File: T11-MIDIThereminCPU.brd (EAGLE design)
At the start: 103.8 x 81.3 mm, 62 parts, among them IC1 UA78M05DCY, IC4 QUAD_OPAMPD, IC5 4069D, J1 DCJ0202, Q1 16MHz, U1 ATMEGA328P-AU

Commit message: Board creation
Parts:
- moved C10 97.1 mm to (3.81, 22.9), turned to 90 degrees
- moved C9 88.7 mm to (91.4, 20.3), turned to 270 degrees
- moved C7 87.8 mm to (22.9, 21.6), turned to 270 degrees
- moved R21 85.9 mm to (97.8, 38.1), turned to 270 degrees
- moved R10 83.2 mm to (86.4, 24.1), turned to 270 degrees
- moved LED1 81.3 mm to (95.2, 76.2)
- moved R3 71.5 mm to (17.8, 24.1), turned to 90 degrees
- moved LED2 70.3 mm to (95.2, 68.6)
- moved R8 70.0 mm to (27.9, 24.1), turned to 270 degrees
- moved JP3 70.0 mm to (27.9, 48.3), turned to 0 degrees
- moved U$4 67.6 mm to (52.1, 24.1), turned to 90 degrees
- moved JP2 64.4 mm to (29.2, 39.4), turned to 0 degrees
- moved C5 64.1 mm to (17.8, 34.3)
- moved LED3 60.1 mm to (95.2, 62.2)
- moved R13 55.3 mm to (85.1, 76.2), turned to 0 degrees
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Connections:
- net GND: now also IC4.12, IC4.13, IC5.11, IC5.13, IC5.5, IC5.9
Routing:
- net GND: track 0.00 -> 535.0 mm
- net +5V: track 0.00 -> 202.9 mm, vias 0 -> 2
- net +12V: track 0.00 -> 154.0 mm
- net ANALOG_IN_1: track 0.00 -> 130.9 mm, vias 0 -> 2
- net MOSI: track 0.00 -> 117.6 mm
- net ANALOG_IN_2: track 0.00 -> 116.7 mm, vias 0 -> 1
- net ANALOG_IN_3: track 0.00 -> 114.7 mm, vias 0 -> 1
- net SIGNAL_OUT_2: track 0.00 -> 70.4 mm, vias 0 -> 1
- net LED_1: track 0.00 -> 66.4 mm
- net PC3: track 0.00 -> 63.6 mm, vias 0 -> 2
- net TX: track 0.00 -> 62.8 mm, vias 0 -> 1
- net ADC6: track 0.00 -> 60.7 mm, vias 0 -> 4
- net SIGNAL_OUT_1: track 0.00 -> 60.4 mm, vias 0 -> 2
- net PC5: track 0.00 -> 57.0 mm, vias 0 -> 1
- net LED_5: track 0.00 -> 56.4 mm
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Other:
- board size 103.8 x 81.3 mm -> 100 x 80 mm

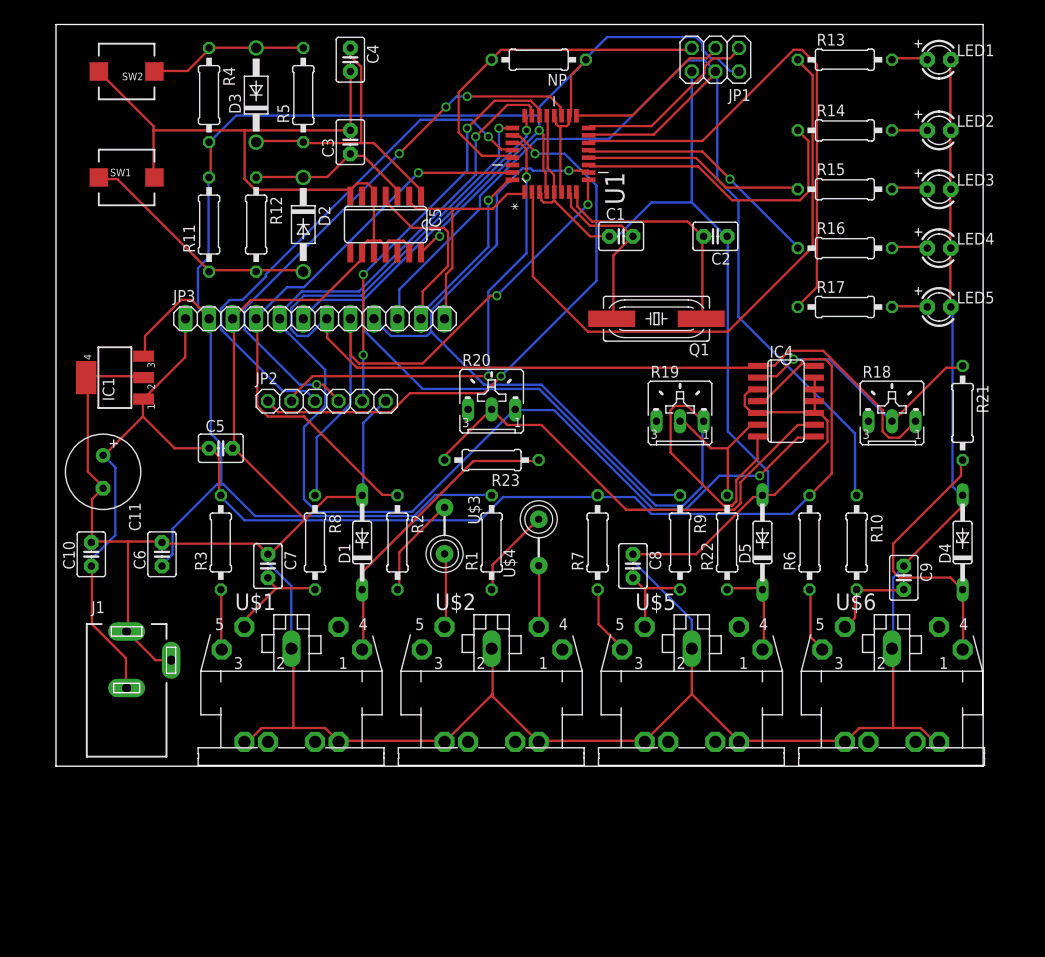
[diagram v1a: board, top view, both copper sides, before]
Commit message: Changed resistors and caps to smd
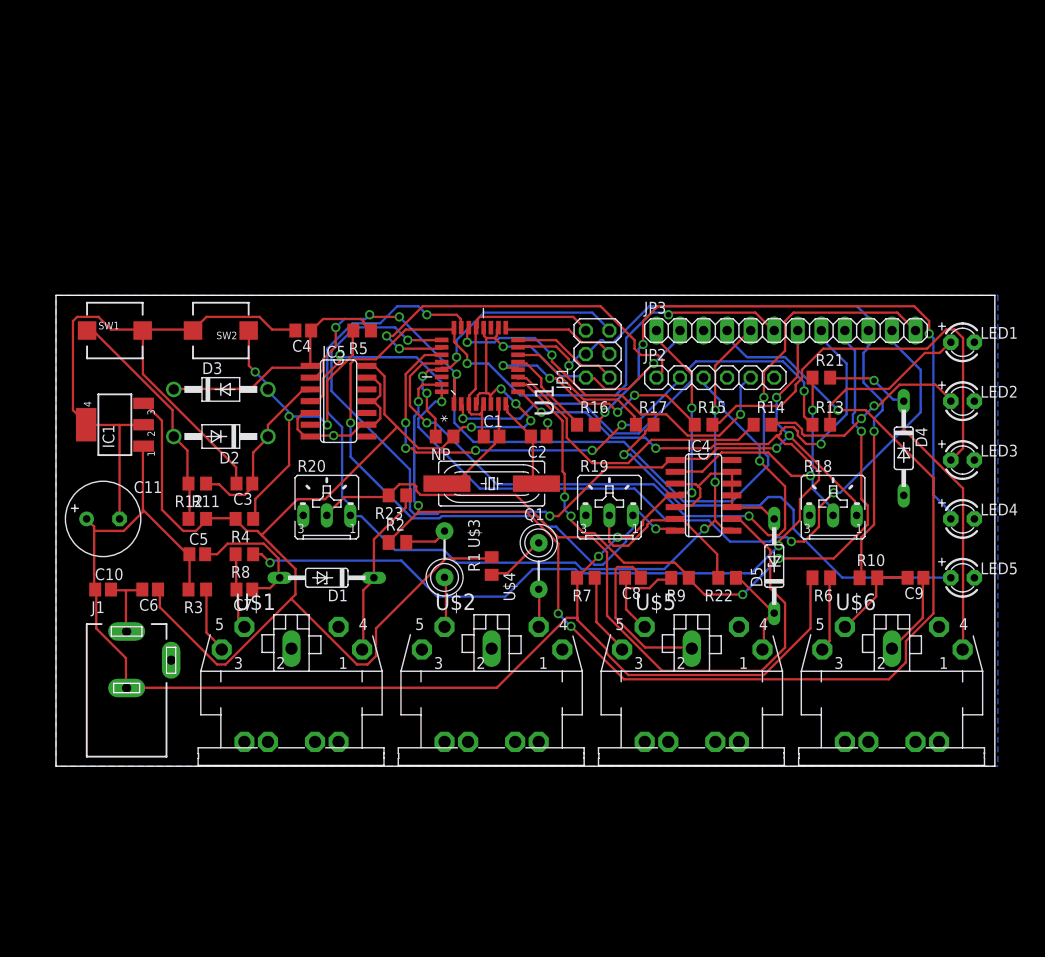
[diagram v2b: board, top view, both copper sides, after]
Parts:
- C1, C10, C2, C3, C4, C5, C6, C7, C8, C9: device capacitor-wima:C2.5-3 -> adafruit:C0805
- NP, R1, R11, R12, R13, R14, R15, R16, R17, R21, R22, R23, R3, R4, R5, R7, R8, R9: device resistor:0207/10 -> resistor:R0805
- R10, R2, R6: device resistor:0207/10 -> resistor:M0805
- moved JP3 50.8 mm to (78.7, 47.0)
- moved R4 45.9 mm to (20.3, 26.7), turned to 180 degrees
- moved JP2 42.0 mm to (71.1, 41.9)
- moved NP 41.9 mm to (41.9, 35.6)
- moved R13 39.5 mm to (82.5, 36.8)
- moved C3 38.6 mm to (20.3, 30.5), turned to 180 degrees
- moved JP1 34.2 mm to (58.4, 44.5), turned to 90 degrees
- moved R16 33.8 mm to (57.1, 36.8)
- moved R14 33.0 mm to (76.2, 36.8)
- moved D3 32.0 mm to (17.8, 40.6), turned to 0 degrees
- moved R11 31.8 mm to (15.2, 26.7), turned to 0 degrees
- moved LED1 30.6 mm to (97.8, 45.7)
- moved SW2 29.7 mm to (17.8, 47.0)
- moved C4 29.6 mm to (26.7, 47.0), turned to 180 degrees
- moved R15 29.6 mm to (69.8, 36.8)
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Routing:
- net GND: track 535.0 -> 195.3 mm, vias 0 -> 2
- net INT1: track 26.5 -> 102.8 mm, vias 0 -> 5
- net TX: track 62.8 -> 136.6 mm, vias 1 -> 5
- net SIGNAL_OUT_1: track 60.4 -> 129.3 mm, vias 2 -> 5
- net INT0: track 38.6 -> 103.1 mm, vias 1 -> 4
- net N$16: track 3.97 -> 67.8 mm, vias 0 -> 3
- net ADC6: track 60.7 -> 0.00 mm, vias 4 -> 0
- net MOSI: track 117.6 -> 73.0 mm, vias 0 -> 2
- net N$17: track 3.89 -> 47.4 mm, vias 0 -> 1
- net N$15: track 4.06 -> 46.4 mm
- net LED_5: track 56.4 -> 16.3 mm
- net N$18: track 52.0 -> 81.3 mm
- net +5V: track 202.9 -> 176.0 mm, vias 2 -> 6
- net ANALOG_IN_1: track 130.9 -> 105.3 mm, vias 2 -> 4
- net N$4: track 17.2 -> 39.6 mm, vias 0 -> 3
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- added copper zone on layer 16, net GND
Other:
- board size 100 x 80 mm -> 101.3 x 50.8 mm

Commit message: Add files via upload
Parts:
- added C12, C13: 0.1u, adafruit:C0805
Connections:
- net +5V: now also C12.1, C13.1
- net GND: now also C12.2, C13.2
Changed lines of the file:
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@@
 <?xml version="1.0" encoding="utf-8"?>
 <!DOCTYPE eagle SYSTEM "eagle.dtd">
-<eagle version="7.6.0">
+<eagle version="7.7.0">
 <drawing>
 <settings>
@@
 <attribute name="OC_NEWARK" value="14R4631" x="45.72" y="43.18" size="1.778" layer="27" rot="R90" display="off"/>
 </element>
+<element name="C12" library="adafruit" package="C0805" value="0.1u" x="-2.54" y="-11.43"/>
+<element name="C13" library="adafruit" package="C0805" value="0.1u" x="-2.54" y="-17.78"/>
 </elements>
 <signals>
@@
 <via x="53.0352" y="37.0332" extent="1-16" drill="0.6096"/>
 <via x="29.9466" y="35.6616" extent="1-16" drill="0.6096"/>
-<wire x1="62.1792" y1="21.4884" x2="66.7766" y2="27.94" width="0" layer="19" extent="1-1"/>
+<contactref element="C12" pad="2"/>
+<contactref element="C13" pad="2"/>
+<wire x1="-1.69" y1="-11.43" x2="-1.69" y2="-17.78" width="0" layer="19" extent="1-1"/>
+<wire x1="20.32" y1="2.62" x2="-1.69" y2="-11.43" width="0" layer="19" extent="1-1"/>
+<wire x1="66.7766" y1="27.94" x2="62.1792" y2="21.4884" width="0" layer="19" extent="1-1"/>
 <wire x1="69.85" y1="46.99" x2="77.47" y2="41.91" width="0" layer="19" extent="1-1"/>
 <wire x1="44.5262" y1="39.0652" x2="34.9758" y2="38.6334" width="0" layer="19" extent="1-1"/>
@@
 <via x="51.2064" y="37.2618" extent="1-16" drill="0.6096"/>
 <via x="44.8056" y="36.576" extent="1-16" drill="0.6096"/>
+<contactref element="C12" pad="1"/>
+<contactref element="C13" pad="1"/>
+<contactref element="C13" pad="1"/>
+<wire x1="-3.39" y1="-11.43" x2="17.3736" y2="10.9728" width="0" layer="19" extent="1-1"/>
+<wire x1="-3.39" y1="-17.78" x2="-3.39" y2="-11.43" width="0" layer="19" extent="1-1"/>
 </signal>
 <signal name="TX">

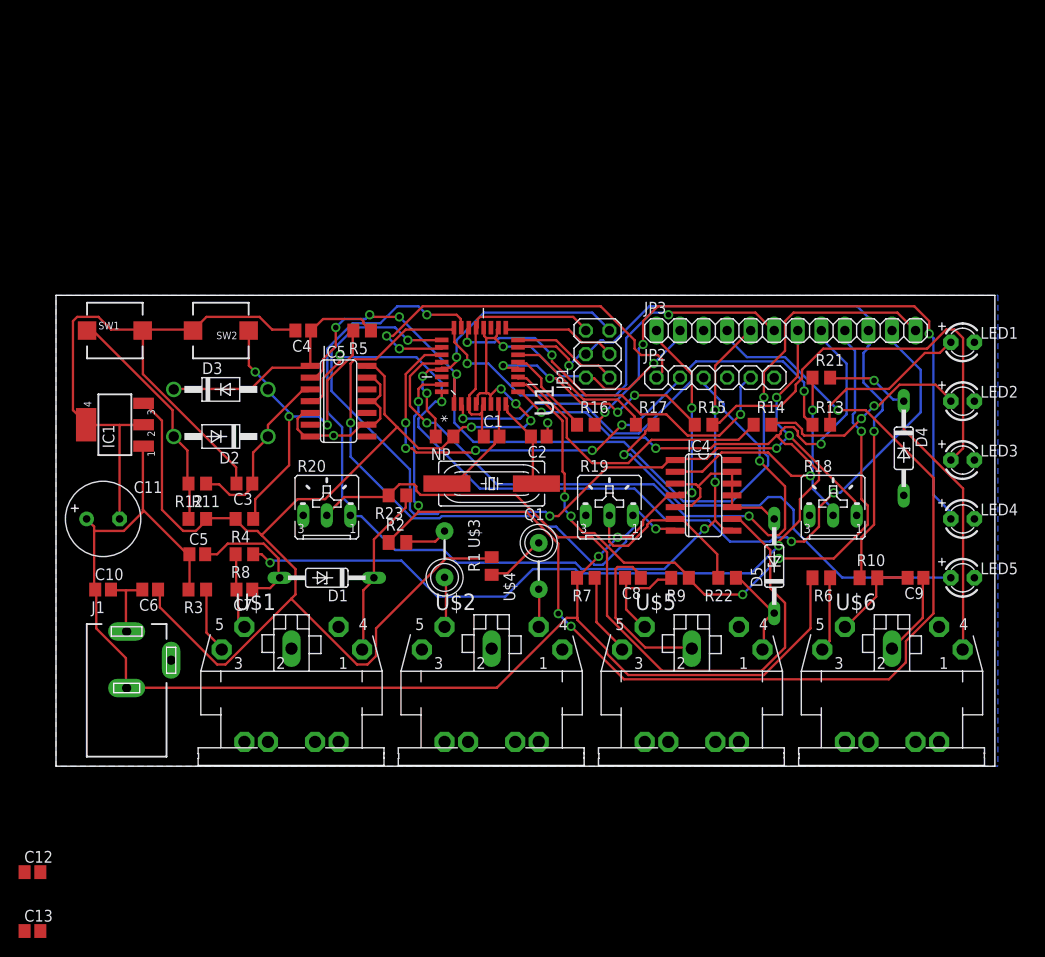
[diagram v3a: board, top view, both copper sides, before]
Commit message: Improved routing, coupling caps added
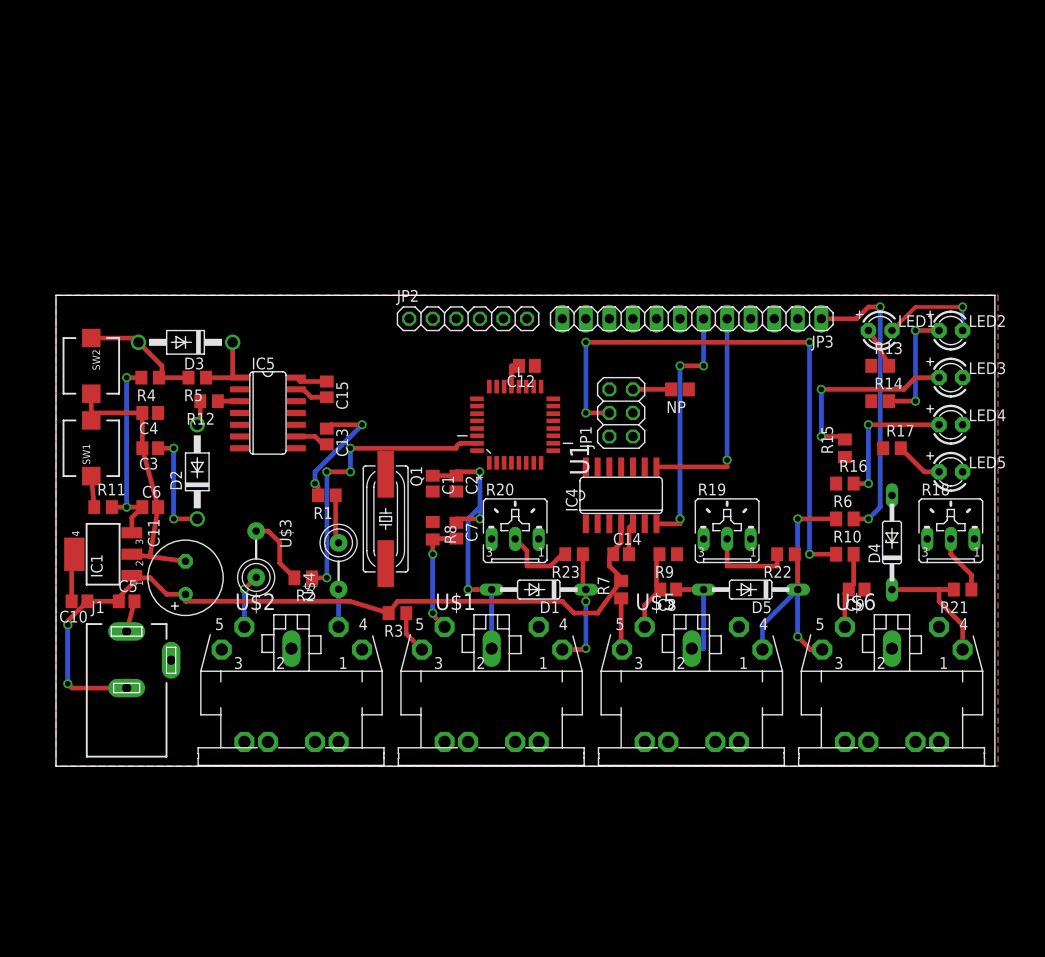
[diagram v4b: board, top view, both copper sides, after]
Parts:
- added C14, C15: 0.1u, adafruit:C0805
- moved C12 76.3 mm to (50.8, 43.2), turned to 180 degrees
- moved C13 62.1 mm to (29.2, 35.6), turned to 270 degrees
- moved R16 28.7 mm to (85.1, 30.5)
- moved R21 27.5 mm to (97.8, 19.1), turned to 180 degrees
- moved JP2 27.4 mm to (44.5, 48.3)
- moved R17 26.8 mm to (90.2, 34.3)
- moved NP 25.9 mm to (67.3, 40.6)
- moved C7 23.7 mm to (43.2, 25.4), turned to 270 degrees
- moved D1 22.9 mm to (52.1, 19.1)
- moved R3 21.7 mm to (36.8, 16.5)
- moved U$1 21.6 mm to (47.0, 0.00)
- moved U$2 21.6 mm to (25.4, 0.00)
- moved U$4 21.6 mm to (30.5, 21.6)
- moved R20 20.5 mm to (49.5, 25.4)
- moved R8 20.5 mm to (40.6, 25.4), turned to 270 degrees
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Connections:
- net +12V: now also C14.1
- net +5V: now also C15.1
- net GND: now also C14.2, C15.2
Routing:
- net +5V: track 176.0 -> 39.4 mm, vias 6 -> 4
- net SIGNAL_OUT_1: track 129.3 -> 0.00 mm, vias 5 -> 0
- net TX: track 136.6 -> 32.0 mm, vias 5 -> 4
- net ANALOG_IN_3: track 103.7 -> 0.00 mm, vias 5 -> 0
- net INT0: track 103.1 -> 0.00 mm, vias 4 -> 0
- net INT1: track 102.8 -> 0.00 mm, vias 5 -> 0
- net GND: track 195.3 -> 106.6 mm, vias 2 -> 4
- net ANALOG_IN_2: track 114.1 -> 27.2 mm, vias 4 -> 3
- net ANALOG_IN_1: track 105.3 -> 23.6 mm, vias 4 -> 1
- net SIGNAL_OUT_2: track 78.4 -> 0.00 mm, vias 5 -> 0
- net PC5: track 73.8 -> 0.00 mm, vias 3 -> 0
- net N$18: track 81.3 -> 8.10 mm
- net N$16: track 67.8 -> 15.6 mm, vias 3 -> 2
- net +12V: track 171.6 -> 119.7 mm
- net LED_1: track 50.8 -> 0.00 mm, vias 2 -> 0
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- added copper zone on layer 1, net GND

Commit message: Improved routing, added coupling caps
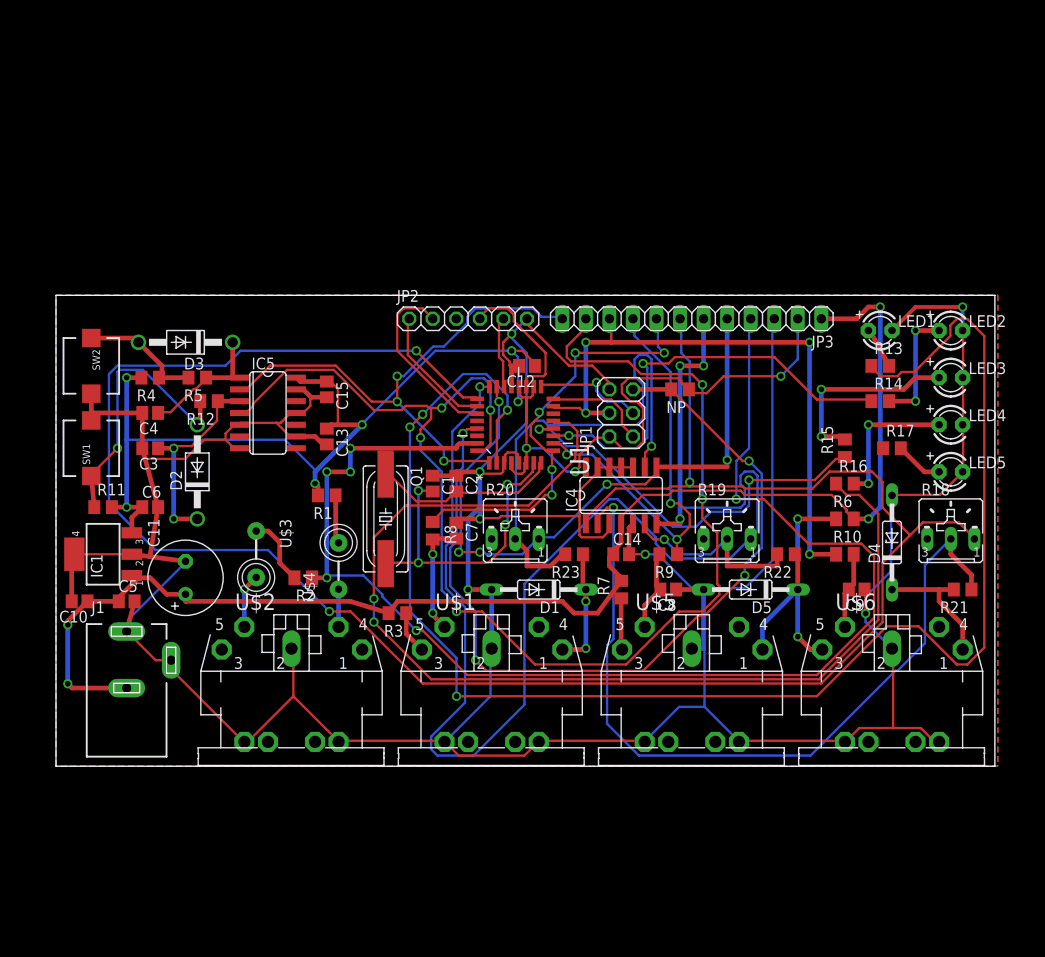
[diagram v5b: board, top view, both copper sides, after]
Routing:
- net GND: track 106.6 -> 447.7 mm, vias 4 -> 7
- net ANALOG_IN_3: track 0.00 -> 230.8 mm, vias 0 -> 3
- net LED_1: track 0.00 -> 165.5 mm, vias 0 -> 4
- net INT0: track 0.00 -> 143.1 mm, vias 0 -> 6
- net ANALOG_IN_2: track 27.2 -> 148.6 mm, vias 3 -> 4
- net +5V: track 39.4 -> 160.4 mm, vias 4 -> 9
- net LED_4: track 0.00 -> 117.6 mm, vias 0 -> 2
- net TX: track 32.0 -> 142.6 mm, vias 4 -> 6
- net RST: track 4.13 -> 91.1 mm, vias 0 -> 4
- net N$19: track 6.38 -> 86.0 mm, vias 0 -> 1
- net INT1: track 0.00 -> 57.6 mm, vias 0 -> 3
- net SIGNAL_OUT_2: track 0.00 -> 47.0 mm, vias 0 -> 3
- net SIGNAL_OUT_1: track 0.00 -> 46.6 mm, vias 0 -> 5
- net N$18: track 8.10 -> 54.7 mm, vias 0 -> 1
- net LED_2: track 0.00 -> 46.3 mm, vias 0 -> 2
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
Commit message: Fixed DRC errors
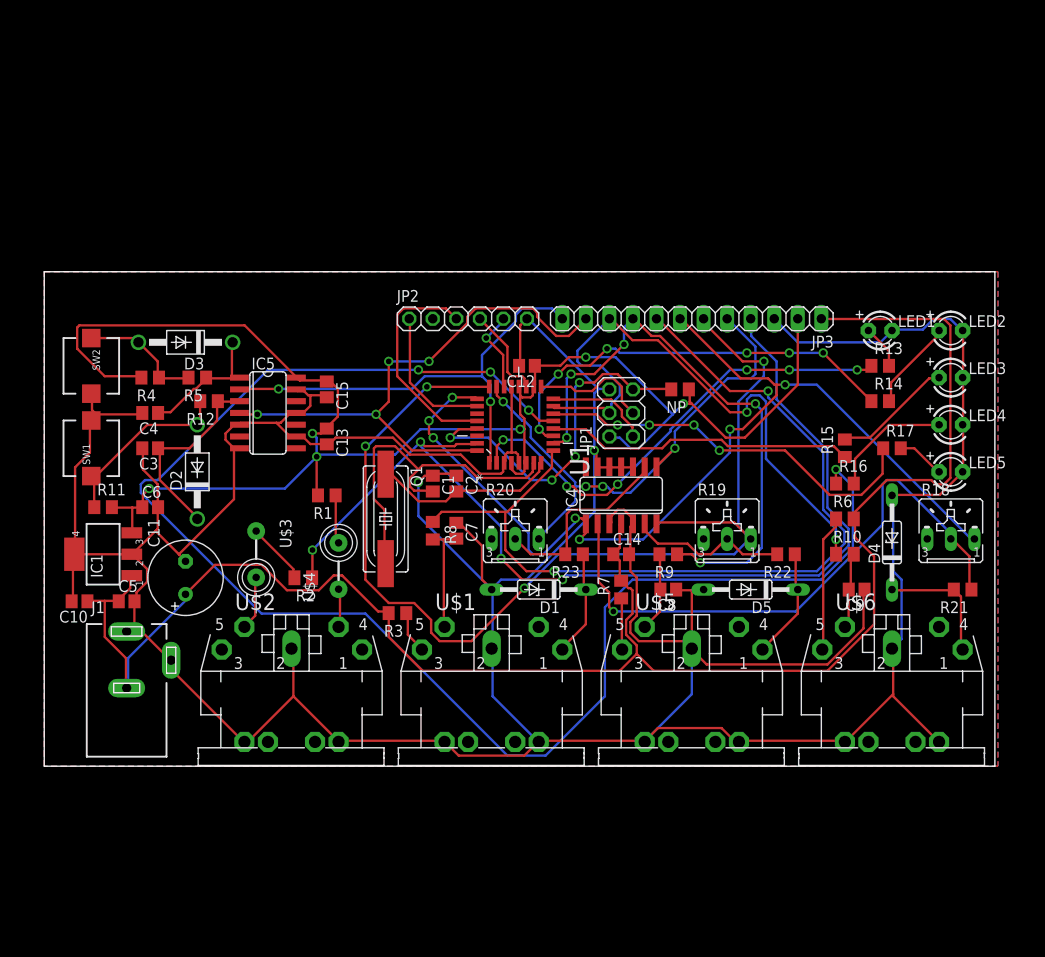
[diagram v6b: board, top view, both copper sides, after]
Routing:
- net ANALOG_IN_3: track 230.8 -> 107.2 mm, vias 3 -> 7
- net LED_1: track 165.5 -> 51.1 mm, vias 4 -> 6
- net INT0: track 143.1 -> 59.9 mm, vias 6 -> 4
- net RST: track 91.1 -> 38.9 mm
- net LED_4: track 117.6 -> 167.0 mm, vias 2 -> 4
- net SIGNAL_OUT_1: track 46.6 -> 95.2 mm, vias 5 -> 2
- net LED_5: track 0.00 -> 42.9 mm, vias 0 -> 4
- net +12V: track 148.0 -> 188.8 mm, vias 4 -> 0
- net GND: track 447.7 -> 485.2 mm, vias 7 -> 2
- net N$18: track 54.7 -> 21.5 mm, vias 1 -> 0
- net TX: track 142.6 -> 110.8 mm, vias 6 -> 4
- net ANALOG_IN_2: track 148.6 -> 120.5 mm
- net PC5: track 0.00 -> 24.4 mm
- net N$19: track 86.0 -> 64.4 mm
- net PC4: track 19.9 -> 0.00 mm
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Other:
- board size 101.3 x 50.8 mm -> 102.5 x 53.3 mm
